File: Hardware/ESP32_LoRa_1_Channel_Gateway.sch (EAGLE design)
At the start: 40 parts, among them J3 USB, J4 QWIIC, J6 U.FL, Q1 MBT3904DW1T1, U1 3.3V, U2 CH340C, U3 ESP-WROOM-32NARROW, U4 RFM95W

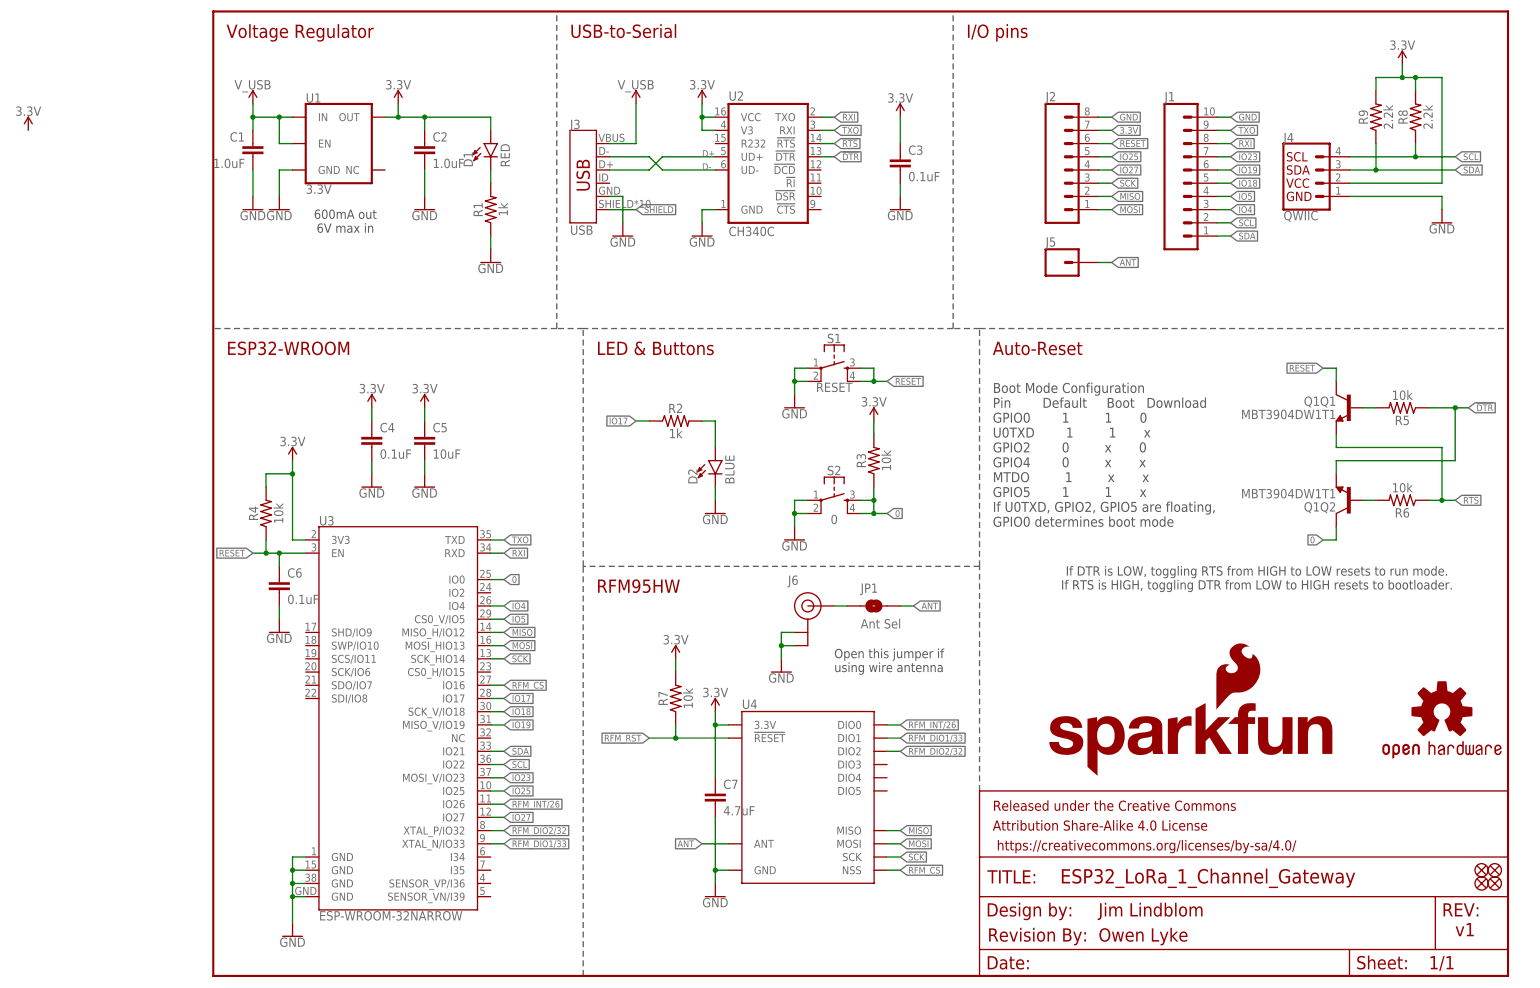
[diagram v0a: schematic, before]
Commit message: Some changes from design review
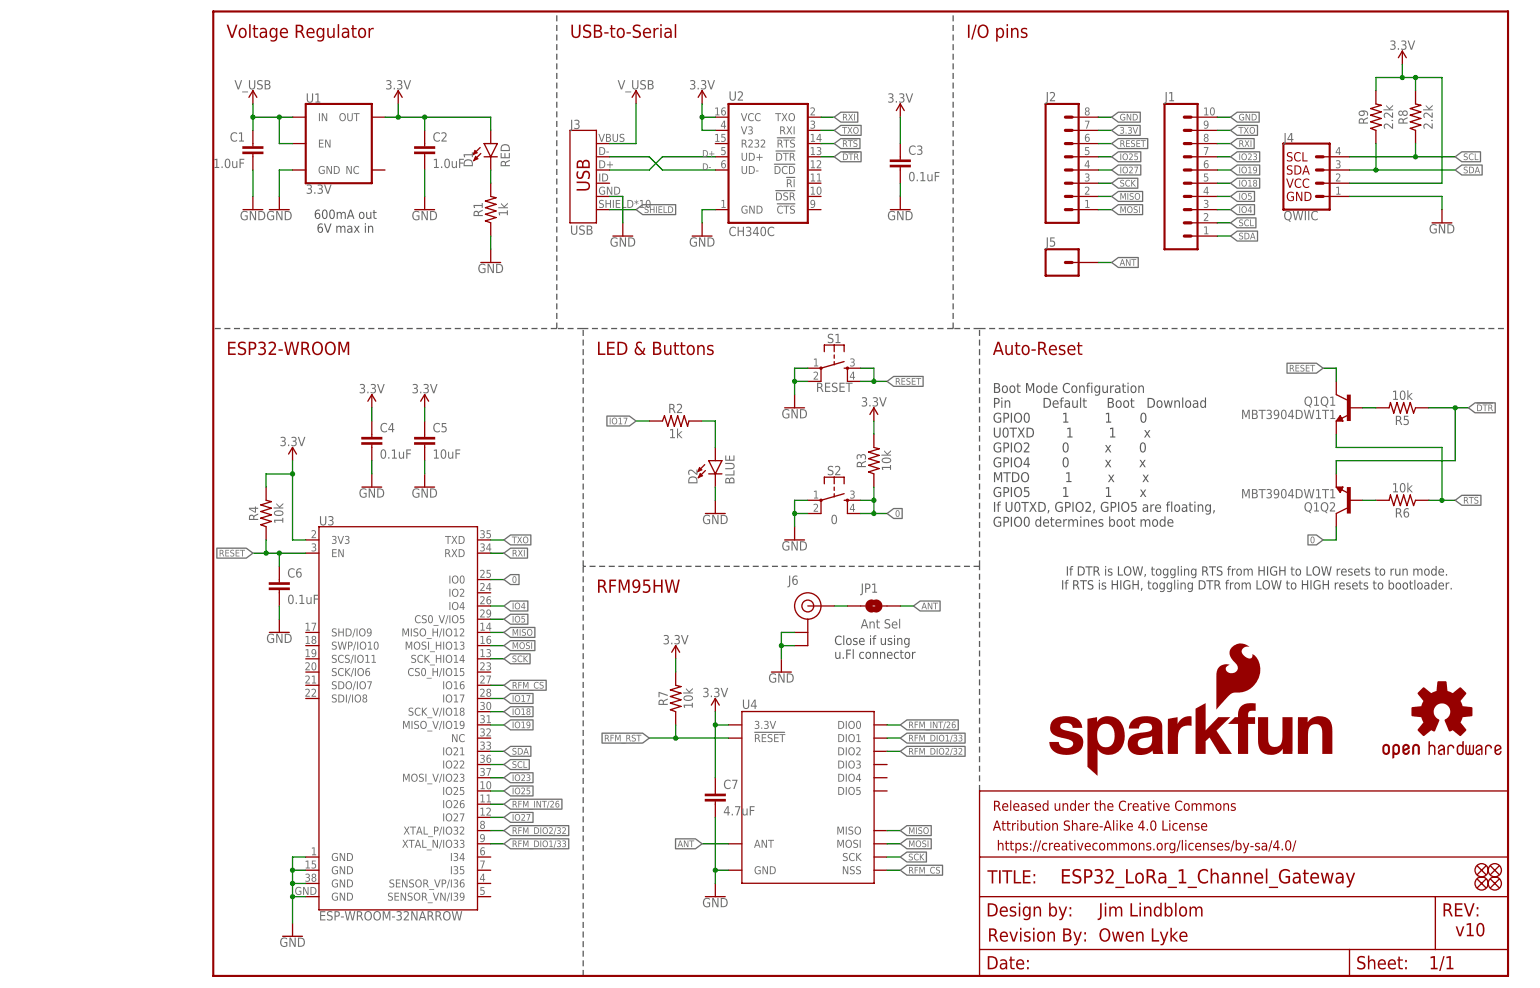
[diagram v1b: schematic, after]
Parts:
- JP1: device SparkFun-Jumpers:JUMPER-SMT_2_NO_SILK -> SparkFun-Jumpers:JUMPER-SMT_2_NO_NO-SILK
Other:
- note added: "Close if using u.Fl connector"
- note added: "v10"
- note removed: "Open this jumper if using wire antenna"
- note removed: "v1"
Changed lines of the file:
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@@
 <drawing>
 <settings>
-<setting alwaysvectorfont="yes"/>
+<setting alwaysvectorfont="no"/>
 <setting verticaltext="up"/>
 </settings>
 <grid distance="0.1" unitdist="inch" unit="inch" style="lines" multiple="1" display="no" altdistance="0.01" altunitdist="inch" altunit="inch"/>
 <layers>
-<layer number="1" name="Top" color="4" fill="1" visible="no" active="no"/>
-<layer number="2" name="Route2" color="1" fill="3" visible="no" active="no"/>
-<layer number="15" name="Route15" color="4" fill="6" visible="no" active="no"/>
-<layer number="16" name="Bottom" color="1" fill="1" visible="no" active="no"/>
-<layer number="17" name="Pads" color="2" fill="1" visible="no" active="no"/>
-<layer number="18" name="Vias" color="2" fill="1" visible="no" active="no"/>
-<layer number="19" name="Unrouted" color="6" fill="1" visible="no" active="no"/>
-<layer number="20" name="Dimension" color="15" fill="1" visible="no" active="no"/>
-<layer number="21" name="tPlace" color="16" fill="1" visible="no" active="no"/>
-<layer number="22" name="bPlace" color="14" fill="1" visible="no" active="no"/>
-<layer number="23" name="tOrigins" color="15" fill="1" visible="no" active="no"/>
-<layer number="24" name="bOrigins" color="15" fill="1" visible="no" active="no"/>
-<layer number="25" name="tNames" color="7" fill="1" visible="no" active="no"/>
-<layer number="26" name="bNames" color="7" fill="1" visible="no" active="no"/>
-<layer number="27" name="tValues" color="7" fill="1" visible="no" active="no"/>
-<layer number="28" name="bValues" color="7" fill="1" visible="no" active="no"/>
+<layer number="1" name="Top" color="4" fill="1" visible="yes" active="no"/>
+<layer number="2" name="Route2" color="1" fill="3" visible="yes" active="no"/>
+<layer number="15" name="Route15" color="4" fill="6" visible="yes" active="no"/>
+<layer number="16" name="Bottom" color="1" fill="1" visible="yes" active="no"/>
+<layer number="17" name="Pads" color="2" fill="1" visible="yes" active="no"/>
+<layer number="18" name="Vias" color="2" fill="1" visible="yes" active="no"/>
+<layer number="19" name="Unrouted" color="6" fill="1" visible="yes" active="no"/>
+<layer number="20" name="Dimension" color="15" fill="1" visible="yes" active="no"/>
+<layer number="21" name="tPlace" color="16" fill="1" visible="yes" active="no"/>
+<layer number="22" name="bPlace" color="14" fill="1" visible="yes" active="no"/>
+<layer number="23" name="tOrigins" color="15" fill="1" visible="yes" active="no"/>
+<layer number="24" name="bOrigins" color="15" fill="1" visible="yes" active="no"/>
+<layer number="25" name="tNames" color="7" fill="1" visible="yes" active="no"/>
+<layer number="26" name="bNames" color="7" fill="1" visible="yes" active="no"/>
+<layer number="27" name="tValues" color="7" fill="1" visible="yes" active="no"/>
+<layer number="28" name="bValues" color="7" fill="1" visible="yes" active="no"/>
 <layer number="29" name="tStop" color="7" fill="3" visible="no" active="no"/>
 <layer number="30" name="bStop" color="7" fill="6" visible="no" active="no"/>
@@
 <layer number="35" name="tGlue" color="7" fill="4" visible="no" active="no"/>
 <layer number="36" name="bGlue" color="7" fill="5" visible="no" active="no"/>
-<layer number="37" name="tTest" color="7" fill="1" visible="no" active="no"/>
-<layer number="38" name="bTest" color="7" fill="1" visible="no" active="no"/>
+<layer number="37" name="tTest" color="7" fill="1" visible="yes" active="no"/>
+<layer number="38" name="bTest" color="7" fill="1" visible="yes" active="no"/>
 <layer number="39" name="tKeepout" color="4" fill="11" visible="no" active="no"/>
 <layer number="40" name="bKeepout" color="1" fill="11" visible="no" active="no"/>
@@
 <layer number="44" name="Drills" color="7" fill="1" visible="no" active="no"/>
 <layer number="45" name="Holes" color="7" fill="1" visible="no" active="no"/>
-<layer number="46" name="Milling" color="3" fill="1" visible="no" active="no"/>
-<layer number="47" name="Measures" color="7" fill="1" visible="no" active="no"/>
-<layer number="48" name="Document" color="7" fill="1" visible="no" active="no"/>
-<layer number="49" name="Reference" color="7" fill="1" visible="no" active="no"/>
-<layer number="50" name="dxf" color="7" fill="1" visible="no" active="no"/>
-<layer number="51" name="tDocu" color="6" fill="1" visible="no" active="no"/>
-<layer number="52" name="bDocu" color="7" fill="1" visible="no" active="no"/>
-<layer number="53" name="tGND_GNDA" color="7" fill="9" visible="no" active="no"/>
-<layer number="54" name="bGND_GNDA" color="1" fill="9" visible="no" active="no"/>
-<layer number="56" name="wert" color="7" fill="1" visible="no" active="no"/>
-<layer number="57" name="tCAD" color="7" fill="1" visible="no" active="no"/>
-<layer number="59" name="tCarbon" color="7" fill="1" visible="no" active="no"/>
-<layer number="60" name="bCarbon" color="7" fill="1" visible="no" active="no"/>
+<layer number="46" name="Milling" color="3" fill="1" visible="yes" active="no"/>
+<layer number="47" name="Measures" color="7" fill="1" visible="yes" active="no"/>
+<layer number="48" name="Document" color="7" fill="1" visible="yes" active="no"/>
+<layer number="49" name="Reference" color="7" fill="1" visible="yes" active="no"/>
+<layer number="50" name="dxf" color="7" fill="1" visible="yes" active="no"/>
+<layer number="51" name="tDocu" color="6" fill="1" visible="yes" active="no"/>
+<layer number="52" name="bDocu" color="7" fill="1" visible="yes" active="no"/>
+<layer number="53" name="tGND_GNDA" color="7" fill="9" visible="yes" active="no"/>
+<layer number="54" name="bGND_GNDA" color="1" fill="9" visible="yes" active="no"/>
+<layer number="56" name="wert" color="7" fill="1" visible="yes" active="no"/>
+<layer number="57" name="tCAD" color="7" fill="1" visible="yes" active="no"/>
+<layer number="59" name="tCarbon" color="7" fill="1" visible="yes" active="no"/>
+<layer number="60" name="bCarbon" color="7" fill="1" visible="yes" active="no"/>
 <layer number="88" name="SimResults" color="9" fill="1" visible="yes" active="yes"/>
 <layer number="89" name="SimProbes" color="9" fill="1" visible="yes" active="yes"/>
@@
 <part name="C3" library="SparkFun-Capacitors" deviceset="0.1UF" device="-0603-25V-5%" value="0.1uF"/>
 <part name="LOGO5" library="SparkFun-Aesthetics" deviceset="SFE_LOGO_NAME_FLAME" device=".1_INCH" value="SFE_LOGO_NAME_FLAME.1_INCH"/>
-<part name="JP1" library="SparkFun-Jumpers" deviceset="JUMPER-SMT_2_NO" device="_SILK" value="Ant Sel"/>
-<part name="SUPPLY15" library="SparkFun-PowerSymbols" deviceset="3.3V" device=""/>
+<part name="JP1" library="SparkFun-Jumpers" deviceset="JUMPER-SMT_2_NO" device="_NO-SILK" value="Ant Sel"/>
 <part name="GND1" library="SparkFun-PowerSymbols" deviceset="GND" device=""/>
 <part name="GND2" library="SparkFun-PowerSymbols" deviceset="GND" device=""/>
@@
 <wire x1="66.04" y1="124.46" x2="66.04" y2="185.42" width="0.2032" layer="97" style="shortdash"/>
 <text x="170.18" y="11.43" size="2.54" layer="94">Jim Lindblom</text>
-<text x="238.76" y="7.62" size="2.54" layer="94">v1</text>
+<text x="238.76" y="7.62" size="2.54" layer="94">v10</text>
 <text x="170.18" y="6.604" size="2.54" layer="94">Owen Lyke</text>
-<text x="119.38" y="58.42" size="1.778" layer="97">Open this jumper if
-using wire antenna</text>
+<text x="119.38" y="60.96" size="1.778" layer="97">Close if using
+u.Fl connector</text>
 </plain>
 <instances>
@@
 <instance part="LOGO5" gate="G$1" x="160.02" y="38.1"/>
 <instance part="JP1" gate="G$1" x="127" y="71.12"/>
-<instance part="SUPPLY15" gate="G$1" x="-35.56" y="162.56"/>
 <instance part="GND1" gate="1" x="7.62" y="147.32"/>
 <instance part="GND2" gate="1" x="12.7" y="147.32"/>

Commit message: Made small fixes
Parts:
- LOGO1: value OSHW-LOGOM -> OSHW-LOGOS; device SparkFun-Aesthetics:OSHW-LOGOM -> SparkFun-Aesthetics:OSHW-LOGOS
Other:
- note added: "Close if using U.FL connector"
- note removed: "Close if using u.Fl connector"
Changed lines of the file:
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@@
 <drawing>
 <settings>
-<setting alwaysvectorfont="no"/>
+<setting alwaysvectorfont="yes"/>
 <setting verticaltext="up"/>
 </settings>
@@
 <part name="J2" library="SparkFun-Connectors" deviceset="CONN_08" device="NO_SILK_FEMALE_PTH"/>
 <part name="R7" library="SparkFun-Resistors" deviceset="10KOHM" device="-0603-1/10W-1%" value="10k"/>
-<part name="LOGO1" library="SparkFun-Aesthetics" deviceset="OSHW-LOGO" device="M"/>
+<part name="LOGO1" library="SparkFun-Aesthetics" deviceset="OSHW-LOGO" device="S" value="OSHW-LOGOS"/>
 <part name="LOGO2" library="SparkFun-Aesthetics" deviceset="REVISION" device=""/>
 <part name="FD1" library="SparkFun-Aesthetics" deviceset="FIDUCIAL" device="1X2"/>
@@
 <text x="170.18" y="6.604" size="2.54" layer="94">Owen Lyke</text>
 <text x="119.38" y="60.96" size="1.778" layer="97">Close if using
-u.Fl connector</text>
+U.FL  connector</text>
 </plain>
 <instances>

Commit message: Fixed checklist issues
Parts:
- removed LOGO5: SFE_LOGO_NAME_FLAME.1_INCH, SparkFun-Aesthetics:SFE_LOGO_NAME_FLAME.1_INCH
- added LOGO3: OSHW-LOGOS, SparkFun-Aesthetics:OSHW-LOGOS
- C2: value 1.0uF -> 0.1uF; device SparkFun-Capacitors:1.0UF-0603-16V-10% -> SparkFun-Capacitors:0.1UF-0603-25V-(+80/-20%)
- C3: device SparkFun-Capacitors:0.1UF-0603-25V-5% -> SparkFun-Capacitors:0.1UF-0603-25V-(+80/-20%)
- C4: value 0.1uF -> 1.0uF; device SparkFun-Capacitors:0.1UF-0603-25V-(+80/-20%) -> SparkFun-Capacitors:1.0UF-0603-16V-10%
- C6: value 0.1uF -> 4.7uF; device SparkFun-Capacitors:0.1UF-0603-25V-(+80/-20%) -> SparkFun-Capacitors:4.7UF-0603-6.3V-(10%)
- C7: value 4.7uF -> 0.1uF; device SparkFun-Capacitors:4.7UF-0603-6.3V-(10%) -> SparkFun-Capacitors:0.1UF-0603-25V-5%
- J1: value (none) -> USB; device SparkFun-Connectors:CONN_10NO_SILK_PTH_FEMALE -> SparkFun-Connectors:USB_MICRO-B_HALF_PTH_MILL
- J2: value (none) -> U.FL; device SparkFun-Connectors:CONN_08NO_SILK_FEMALE_PTH -> SparkFun-Connectors:U.FL
- J3: value USB -> (none); device SparkFun-Connectors:USB_MICRO-B_HALF_PTH_MILL -> SparkFun-Connectors:CONN_01PTH_NO_SILK_YES_STOP
- J4: value QWIIC -> (none); device SparkFun-Connectors:QWIIC_CONNECTORJS-1MM -> SparkFun-Connectors:CONN_08NO_SILK_FEMALE_PTH
- J5: device SparkFun-Connectors:CONN_01PTH_NO_SILK_YES_STOP -> SparkFun-Connectors:CONN_10NO_SILK_PTH_FEMALE
- J6: value U.FL -> QWIIC; device SparkFun-Connectors:U.FL -> SparkFun-Connectors:QWIIC_CONNECTORJS-1MM
- LOGO1: value OSHW-LOGOS -> REVISION; device SparkFun-Aesthetics:OSHW-LOGOS -> SparkFun-Aesthetics:REVISION
- LOGO2: value REVISION -> SFE_LOGO_NAME_FLAME.1_INCH; device SparkFun-Aesthetics:REVISION -> SparkFun-Aesthetics:SFE_LOGO_NAME_FLAME.1_INCH
- Q1: device esp32-thing-temp:MBT3904DW1T1 -> SparkFun-DiscreteSemi:TRANS_NPN_DUAL-MBT3904DW1T1
- R1: value 1k -> 10k; device SparkFun-Resistors:1KOHM-0603-1/10W-1% -> SparkFun-Resistors:10KOHM-0603-1/10W-1%
- R3: value 10k -> 1k; device SparkFun-Resistors:10KOHM-0603-1/10W-1% -> SparkFun-Resistors:1KOHM-0603-1/10W-1%
- R6: value 10k -> 2.2k; device SparkFun-Resistors:10KOHM-0603-1/10W-1% -> SparkFun-Resistors:2.2KOHM-0603-1/10W-1%
- R8: value 2.2k -> 10k; device SparkFun-Resistors:2.2KOHM-0603-1/10W-1% -> SparkFun-Resistors:10KOHM-0603-1/10W-1%
- U2: value CH340C -> ESP-WROOM-32NARROW; device SparkFun-IC-Comms:CH340C -> SparkFun-RF:ESP-WROOM-32NARROW
- U3: value ESP-WROOM-32NARROW -> CH340C; device esp32_lora_gateway:ESP-WROOM-32NARROW -> SparkFun-IC-Comms:CH340C
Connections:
- net !DTR: now also R7.1, U3.!DTR; no longer R5.1, U2.!DTR
- net !RTS: now also R8.1, U3.!RTS; no longer R6.1, U2.!RTS
- net 0: now also R5.1, U2.IO0; no longer R3.1, U3.IO0
- net 3.3V: now also C6.1, J4.7, J6.2, R1.2, R5.2, R6.2, U2.3V3, U3.V3, U3.VCC; no longer C2.1, J2.7, J4.2, R3.2, R7.2, R8.2, U2.V3, U2.VCC, U3.3V3
- net ANT: now also J3.1; no longer J5.1
- net D+: now also J1.D+, U3.UD+; no longer J3.D+, U2.UD+
- net D-: now also J1.D-, U3.UD-; no longer J3.D-, U2.UD-
- net GND: now also J1.GND, J2.GND@0, J2.GND@1, J4.8, J5.10, J6.1, R2.1, U2.GND@1, U2.GND@15, U2.GND@38; no longer J1.10, J2.8, J3.GND, J4.1, J6.GND@0, J6.GND@1, R1.1, U3.GND@1, U3.GND@15, U3.GND@38
- net IO17: now also R3.1, U2.IO17; no longer R2.1, U3.IO17
- net IO18: now also J5.5, U2.SCK_V/IO18; no longer J1.5, U3.SCK_V/IO18
- net IO19: now also J5.6, U2.MISO_V/IO19; no longer J1.6, U3.MISO_V/IO19
- net IO23: now also J5.7, U2.MOSI_V/IO23; no longer J1.7, U3.MOSI_V/IO23
- net IO25: now also J4.5, U2.IO25; no longer J2.5, U3.IO25
- net IO27: now also J4.4, U2.IO27; no longer J2.4, U3.IO27
- net IO4: now also J5.3, U2.IO4; no longer J1.3, U3.IO4
- net IO5: now also J5.4, U2.CS0_V/IO5; no longer J1.4, U3.CS0_V/IO5
- net MISO: now also J4.2, U2.MISO_H/IO12; no longer J2.2, U3.MISO_H/IO12
- net MOSI: now also J4.1, U2.MOSI_H/IO13; no longer J2.1, U3.MOSI_HIO13
- net N$1: now also R2.2; no longer R1.2
- net N$10: now also R7.2; no longer R5.2
- net N$12: now also R8.2; no longer R6.2
- net N$2: now also R3.2; no longer R2.2
- net N$3: now also J2.SIGNAL; no longer J6.SIGNAL
- net RESET: now also C2.1, J4.6, R1.1, U2.EN; no longer C6.1, J2.6, R4.1, U3.EN
- net RFM_CS: now also U2.IO16; no longer U3.IO16
- net RFM_DIO1/33: now also U2.XTAL_N/IO33; no longer U3.XTAL_N/IO33
- net RFM_DIO2/32: now also U2.XTAL_P/IO32; no longer U3.XTAL_P/IO32
- net RFM_INT/26: now also U2.IO26; no longer U3.IO26
- net RFM_RST: now also R4.1; no longer R7.1
- net RXI: now also J5.8, U2.RXD, U3.TXO; no longer J1.8, U2.TXO, U3.RXD
- net SCK: now also J4.3, U2.SCK_H/IO14; no longer J2.3, U3.SCK_HIO14
- net SCL: now also J5.2, J6.4, R9.1, U2.IO22; no longer J1.2, J4.4, R8.1, U3.IO22
- net SDA: now also J5.1, J6.3, R6.1, U2.IO21; no longer J1.1, J4.3, R9.1, U3.IO21
- net SHIELD: now also J1.SHIELD; no longer J3.SHIELD
- net TXO: now also J5.9, U2.TXD, U3.RXI; no longer J1.9, U2.RXI, U3.TXD
- net V_USB: now also J1.VBUS; no longer J3.VBUS
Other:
- moved on the sheet: C2, C3, C4, C6, C7, R1, R2, R3, R4, R5, R6, R7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
